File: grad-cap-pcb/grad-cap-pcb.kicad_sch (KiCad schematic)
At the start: 0 parts

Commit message: added many things
added: mux
counter
signal gen - still needs r1 and r2 values
power management
kicad symbol library - footprints not assigned
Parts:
- added C1: C_Small_US, symbol Device:C_Small_US
- added C2: C_Small, symbol Device:C_Small
- added J1: B02B-XASK-1LFSN, CONN_B02B-XASK-1LFSN_JST, symbol 1X02_JST:B02B-XASK-1LFSN
- added R1, R6, R7, R8, R9: 10K, symbol Device:R_Small_US
- added R10: 10k, symbol Device:R_Small_US
- added R4, R5: R_Small_US, symbol Device:R_Small_US
- added U10: CD74HC154M96, DW24, symbol CD74HC154M96_4_16-MUX:CD74HC154M96
- added U4, U5: MC74HC73ADR2G, SOIC-14_NB_ONS, symbol MC74HC73ADR2G_JK-FLIPFLOP:MC74HC73ADR2G
- added U7: ICM7555xB, Package_SO:SOIC-8_3.9x4.9mm_P1.27mm, symbol Timer:ICM7555xB
- added U9: XC6220B211MR-G, SOT-25_TOR, symbol XC6220B21MR_2.1V-1A-REG:XC6220B211MR-G
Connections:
- new net: R1.1, U10.18 (*E1), U10.19 (*E2)
- new net: R10.2, U9.3 (CE)
- new net: R6.2, U5.2 (RESET1), U5.3 (K1)
- new net: R8.2, U4.10 (K2), U4.14 (J1)
- new net: R7.2, U4.2 (RESET1), U4.3 (K1), U4.6 (RESET2), U4.7 (J2)
- new net: R9.2, U5.14 (J1)
- new net: C2.1, U7.5 (CV)
- new net: R4.1, R5.2, U7.7 (DIS)
- new net: C1.1, R4.2, U7.2 (TR), U7.6 (THR)
- new net +2V2: U9.5 (VOUT)
- new net +3.3V: J1.1, R10.1, R5.1, R6.1, R7.1, R8.1, R9.1, U10.24 (VCC), U4.4 (VCC), U5.4 (VCC), U7.4 (R), U7.8 (VCC), U9.1 (VIN)
- new net 0: U10.1 (*Y0)
- new net 1: U10.2 (*Y1)
- new net 10: U10.11 (*Y10)
- new net 11: U10.13 (*Y11)
- new net 12: U10.14 (*Y12)
- new net 13: U10.15 (*Y13)
- new net 14: U10.16 (*Y14)
- new net 15: U10.17 (*Y15)
- new net 2: U10.3 (*Y2)
- new net 3: U10.4 (*Y3)
- new net 4: U10.5 (*Y4)
- new net 5: U10.6 (*Y5)
- new net 6: U10.7 (*Y6)
- new net 7: U10.8 (*Y7)
- new net 8: U10.9 (*Y8)
- new net 9: U10.10 (*Y9)
- new net CLOCK1: U10.23 (A0), U4.1 (CLOCK1), U7.3 (Q)
- new net CLOCK2: U10.22 (A1), U4.12 (Q1), U4.5 (CLOCK2)
- new net CLOCK3: U10.21 (A2), U4.9 (Q2), U5.1 (CLOCK1)
- new net CLOCK4: U10.20 (A3), U5.12 (Q1)
- new net GND: C1.2, C2.2, J1.2, R1.2, U10.12 (GND), U4.11 (GND), U5.11 (GND), U5.6 (RESET2), U7.1 (GND), U9.2 (VSS)
- no-connect marks 0 -> 8
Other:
- removed sheet adder
- removed sheet demux
- removed sheet pulse_gen
- note added: "2 pin JST from battery"
- note added: "3V7 -> 2V1"
- note added: "CLOCK OUTPUT"
- note added: "INPUT FROM 555"
- note added: "R1"
- note added: "R2"
- note added: "adder"
- note added: "linear reg"
- note added: "mux"
- note added: "power in"
- note added: "power management"
- note added: "pulse generator"

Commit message: edited layout
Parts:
- removed U10: CD74HC154M96, DW24, symbol CD74HC154M96_4_16-MUX:CD74HC154M96
- added U10: CD74HC154M96, GRAD-CAP:CD74HC154M96_4-16-MUX, symbol CD74HC154M96_4-16-MUX:CD74HC154M96
- C1, C2: footprint (none) -> Capacitor_SMD:C_0805_2012Metric_Pad1.18x1.45mm_HandSolder
- J1: footprint CONN_B02B-XASK-1LFSN_JST -> GRAD-CAP:1X02JST
- R1, R10, R4, R5, R6, R7, R8, R9: footprint (none) -> Resistor_SMD:R_0805_2012Metric_Pad1.20x1.40mm_HandSolder
- U4, U5: footprint SOIC-14_NB_ONS -> GRAD-CAP:MC74HC73ADR2G_JK-FLIPFLOP
- U9: footprint SOT-25_TOR -> GRAD-CAP:XC6220B21MR_2.1V-1A-REG
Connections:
- net +3.3V: now also U10.24 (VCC)
- net 0: now also U10.1 (*Y0)
- net 1: now also U10.2 (*Y1)
- net 10: now also U10.11 (*Y10)
- net 11: now also U10.13 (*Y11)
- net 12: now also U10.14 (*Y12)
- net 13: now also U10.15 (*Y13)
- net 14: now also U10.16 (*Y14)
- net 15: now also U10.17 (*Y15)
- net 2: now also U10.3 (*Y2)
- net 3: now also U10.4 (*Y3)
- net 4: now also U10.5 (*Y4)
- net 5: now also U10.6 (*Y5)
- net 6: now also U10.7 (*Y6)
- net 7: now also U10.8 (*Y7)
- net 8: now also U10.9 (*Y8)
- net 9: now also U10.10 (*Y9)
- net CLOCK1: now also U10.23 (A0)
- net CLOCK2: now also U10.22 (A1)
- net CLOCK3: now also U10.21 (A2)
- net CLOCK4: now also U10.20 (A3)
- net GND: now also U10.12 (GND)
- net at R1.1: now also U10.18 (*E1), U10.19 (*E2)
- net u5-pu-r1: now reaches R6.2, U5.2 (RESET1), U5.3 (K1)
- net u4-pu-r2: now reaches R8.2, U4.10 (K2), U4.14 (J1)
- net u4-pu-r1: now reaches R7.2, U4.2 (RESET1), U4.3 (K1), U4.6 (RESET2), U4.7 (J2)
- net u5-pu-r2: now reaches R9.2, U5.14 (J1)
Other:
- moved on the sheet: R1

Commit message: routed traces, added resistors
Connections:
- net pd_r_18/19: now reaches R1.1, U10.18 (*E1), U10.19 (*E2)
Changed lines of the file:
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@@
+		)
+	)
+	(label "pd_r_18{slash}19"
+		(at 331.47 76.2 0)
+		(effects
+			(font
+				(size 1.27 1.27)
+			)
+			(justify left bottom)
 		)
 	)

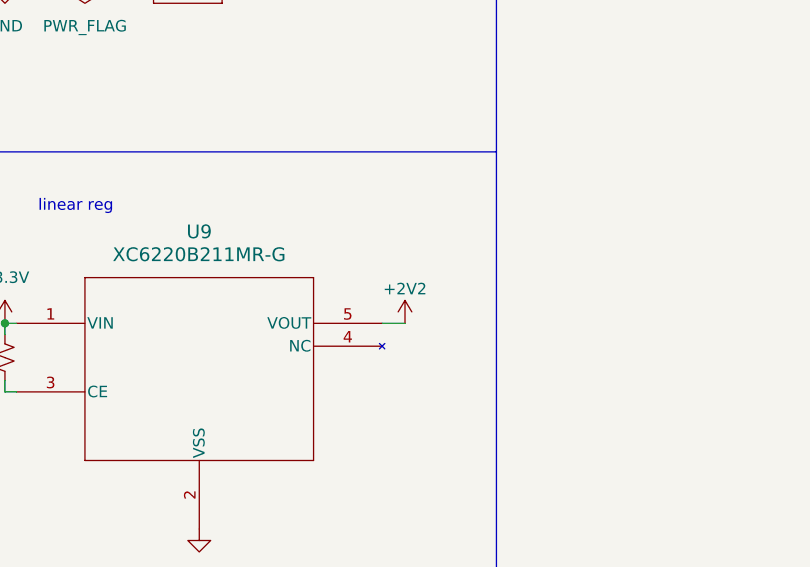
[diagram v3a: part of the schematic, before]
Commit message: screw it were making it 8 frames, 16 is too mcuh
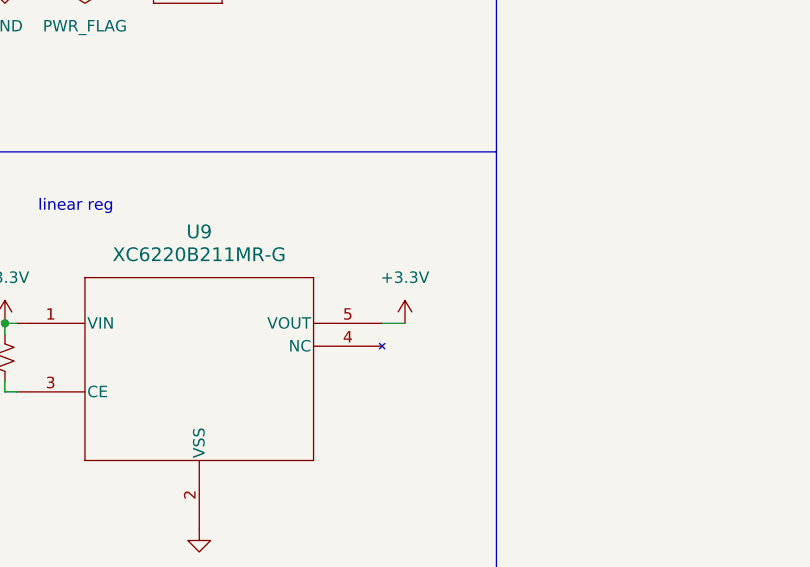
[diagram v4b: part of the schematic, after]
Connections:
- net +2V2 is gone; now on net +3.3V: U9.5 (VOUT)
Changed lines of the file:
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@@
 	)
 	(symbol
-		(lib_id "power:+2V5")
+		(lib_id "power:+3.3V")
 		(at 88.9 200.66 0)
 		(unit 1)
@@
 		(dnp no)
 		(fields_autoplaced yes)
-		(property "Reference" "#PWR041"
+		(property "Reference" "#PWR41"
 			(at 88.9 204.47 0)
 			(effects
@@
 			)
 		)
-		(property "Value" "+2V2"
-			(at 88.9 196.85 0)
+		(property "Value" "+3.3V"
+			(at 88.9 195.58 0)
 			(effects
 				(font
@@
 			)
 		)
-		(property "Description" "Power symbol creates a global label with name \"+2V5\""
+		(property "Description" "Power symbol creates a global label with name \"+3.3V\""
 			(at 88.9 200.66 0)
 			(effects
@@
 			(project "grad-cap-pcb"
 				(path "/e928cd2e-687b-4f0f-a80d-e766cc3f22d6"
-					(reference "#PWR041")
+					(reference "#PWR41")
 					(unit 1)
 				)
